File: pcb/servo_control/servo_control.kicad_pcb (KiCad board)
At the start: 2 copper layers, 94.6 x 66.7 mm, 62 parts, among them J1 Jack-DC, J10 Conn_01x03_Female, J11 Conn_01x03_Female, J12 Conn_01x03_Female, J13 Conn_01x03_Female, J14 Conn_01x03_Female, J15 Conn_01x03_Female, J16 Conn_01x03_Female, J17 Conn_01x03_Female, J18 Conn_01x03_Female, J19 Conn_01x03_Female, J2 YLIDAR X4, J20 Conn_01x03_Female, J21 Conn_01x06_Male, J22 GY-87, J3 Conn_01x03_Female, J4 Conn_01x03_Female, J5 Conn_01x03_Female, J6 Conn_01x03_Female, J7 Conn_01x03_Female, J8 Conn_01x03_Female, J9 Conn_01x03_Female, SW1 ESP_PROG, SW2 ESP_RST, U1 PCA9685PW, U2 LM317-3.3_SOT-223, U3 ESP32-WROOM-32, U4 MCP73213-A6SI/MF, U5 PCA9685PW, U6 LM317-5_SOT-223, U7 LT1085-ADJ

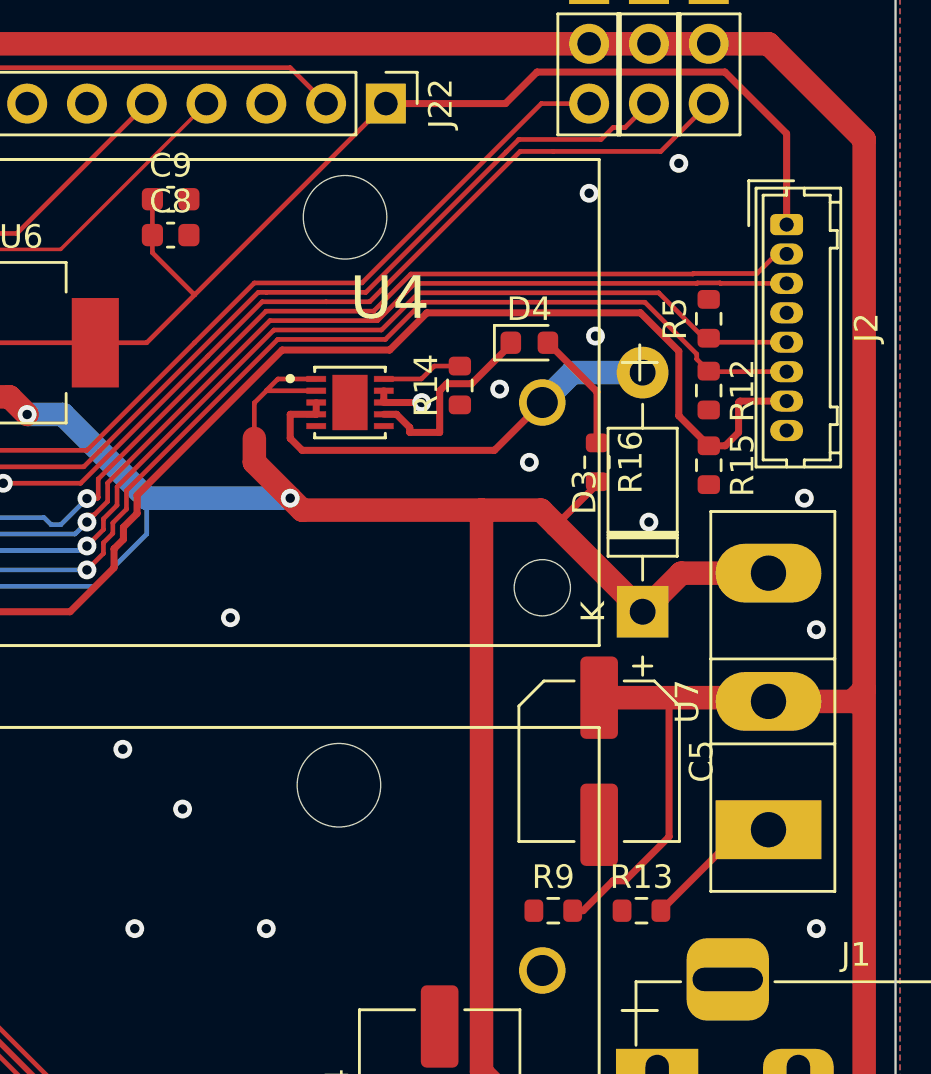
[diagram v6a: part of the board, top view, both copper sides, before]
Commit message: fix gnd 5v + adjust 6V
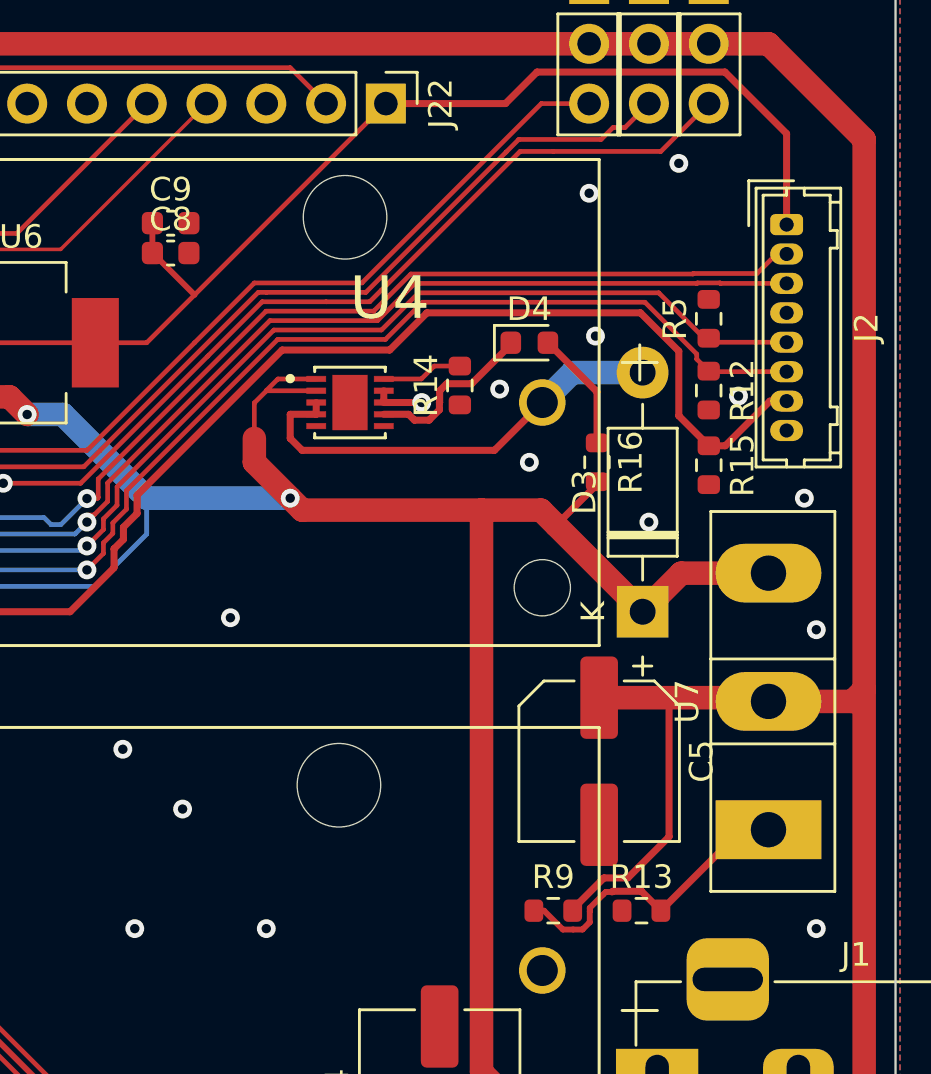
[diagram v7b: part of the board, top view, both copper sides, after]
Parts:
- moved C9 1.02 mm to (165.1, 53.3)
- moved C8 0.76 mm to (165.1, 54.6)
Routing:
- net Net-(R13-Pad2): track 6.00 -> 13.1 mm
- net Net-(D4-Pad1): track 8.50 -> 7.38 mm
- net 5V: track 85.6 -> 84.6 mm
- net M_EN: track 93.0 -> 92.2 mm
- net GND: vias 39 -> 40

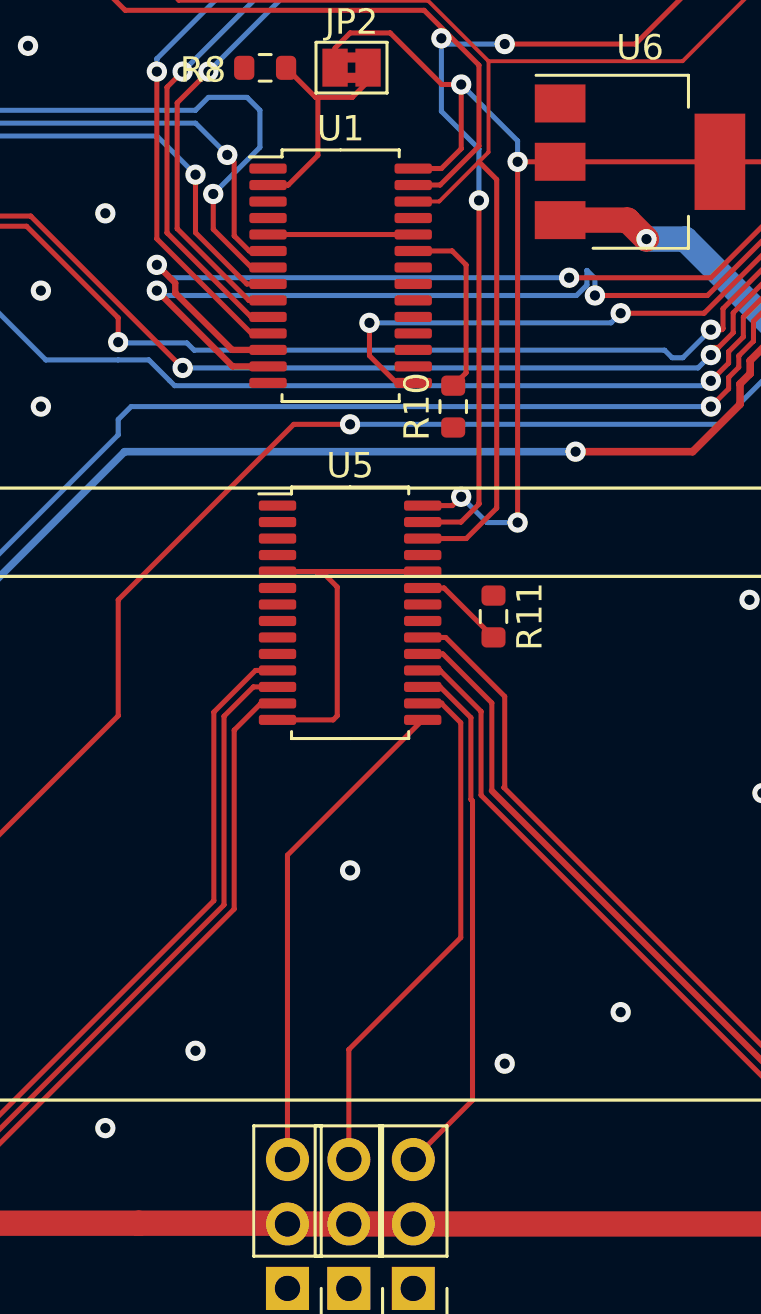
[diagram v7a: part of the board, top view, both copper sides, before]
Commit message: update mcp9586 for i2c address
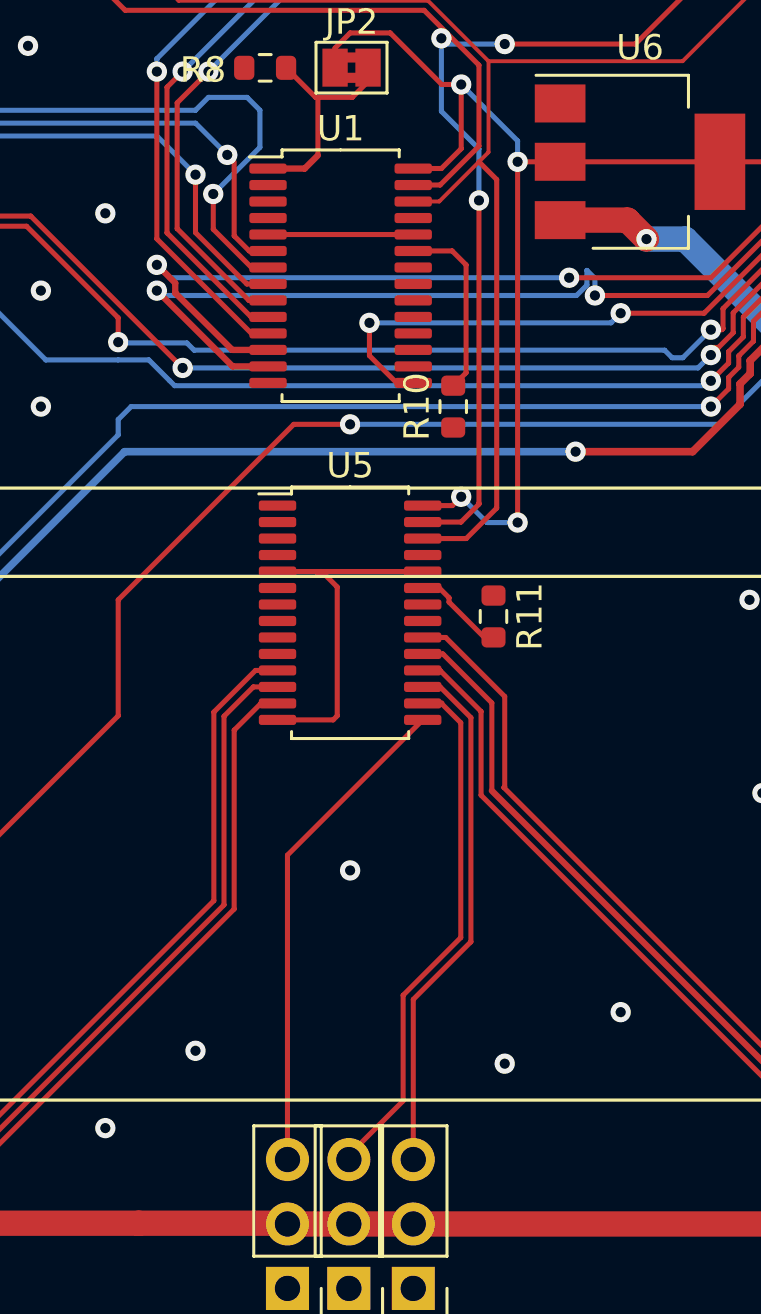
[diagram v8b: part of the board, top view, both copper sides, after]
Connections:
- JP2 pad 2: FIRST_A1 -> FIRST_A0
- R8 pad 2: FIRST_A1 -> FIRST_A0
- U1 pad 2: FIRST_A1 -> GND
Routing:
- net FIRST_A1: track 9.26 -> 0.00 mm
- net FIRST_A0: track 0.00 -> 8.99 mm
